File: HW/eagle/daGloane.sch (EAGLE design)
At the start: 61 parts, among them IC1 MCP1252-33X50, U1 STM32F10XTXU6, X2 SPARKFUN-CONNECTORS_USB-MICROB

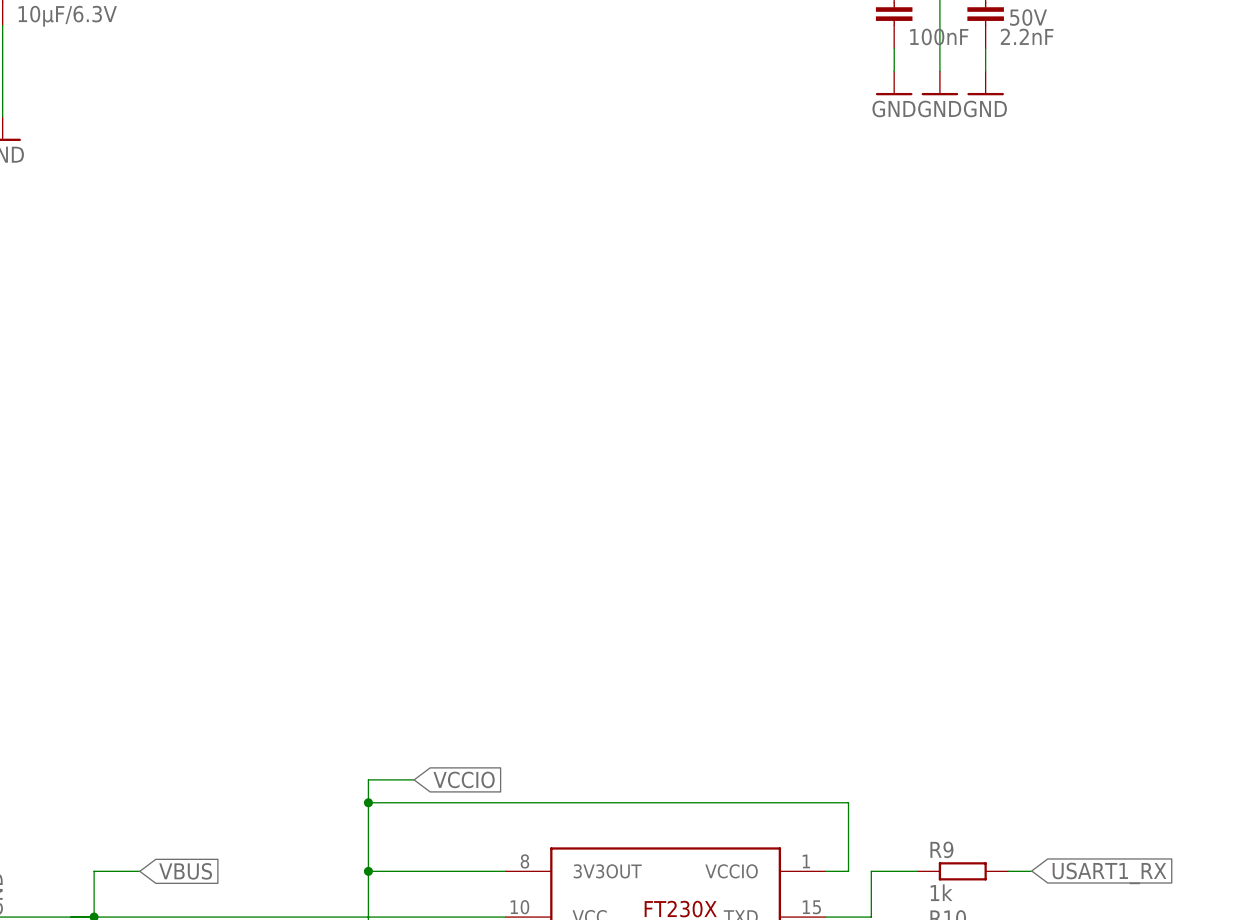
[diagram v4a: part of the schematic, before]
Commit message: Added Bluetooth module
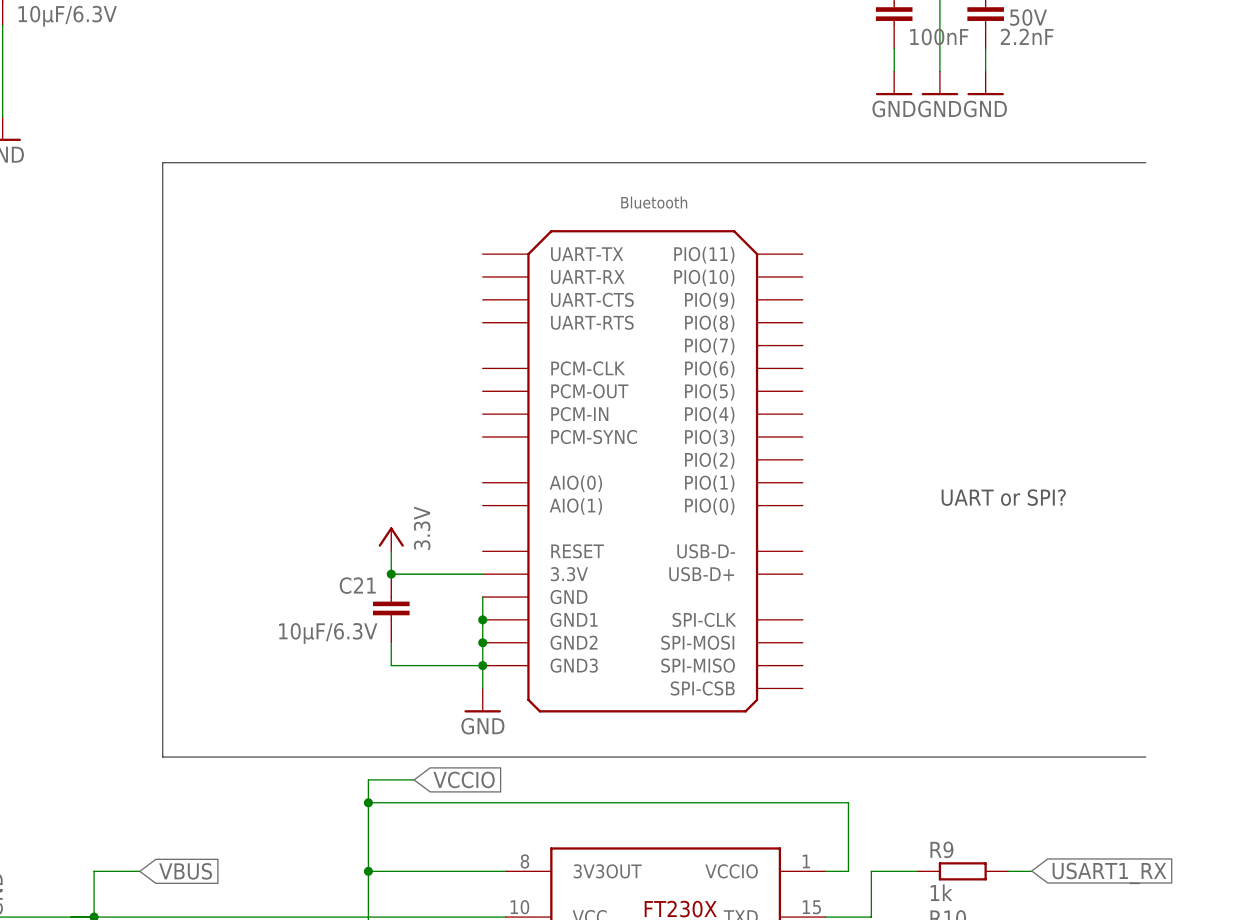
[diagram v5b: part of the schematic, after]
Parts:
- added C21: 10µF/6.3V, rcl:C-EUC0805
- added U$5: BLUETOOTH, daGloane:BLUETOOTH
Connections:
- net GND: now also C21.2, U$5.GND, U$5.GND1, U$5.GND2, U$5.GND3
- net VCC: now also C21.1, U$5.3.3V
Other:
- note added: "UART or SPI?"
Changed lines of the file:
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@@
 <layer number="95" name="Names" color="7" fill="1" visible="yes" active="yes"/>
 <layer number="96" name="Values" color="7" fill="1" visible="yes" active="yes"/>
-<layer number="97" name="Info" color="7" fill="1" visible="no" active="yes"/>
+<layer number="97" name="Info" color="7" fill="1" visible="yes" active="yes"/>
 <layer number="98" name="Guide" color="6" fill="1" visible="no" active="yes"/>
 <layer number="99" name="Anatomie" color="7" fill="1" visible="no" active="yes"/>
@@
 <part name="GND6" library="supply1" deviceset="GND" device=""/>
 <part name="X2" library="daGloane" deviceset="SPARKFUN-CONNECTORS_USB" device="-MICROB"/>
+<part name="U$5" library="daGloane" deviceset="BLUETOOTH" device=""/>
+<part name="C21" library="rcl" deviceset="C-EU" device="C0805" value="10µF/6.3V"/>
+<part name="3.3V1" library="supply1" deviceset="VCC" device="" value="3.3V"/>
+<part name="GND17" library="supply1" deviceset="GND" device=""/>
 </parts>
 <sheets>
@@
 <text x="215.9" y="15.24" size="2.54" layer="91">Filter hinter charge pump?</text>
 <text x="111.76" y="88.9" size="1.778" layer="91" rot="MR0">boot1</text>
+<wire x1="373.38" y1="147.32" x2="264.16" y2="147.32" width="0.1524" layer="97"/>
+<wire x1="264.16" y1="147.32" x2="264.16" y2="81.28" width="0.1524" layer="97"/>
+<wire x1="264.16" y1="81.28" x2="373.38" y2="81.28" width="0.1524" layer="97"/>
+<text x="350.52" y="109.22" size="1.778" layer="97">UART or SPI?</text>
 </plain>
 <instances>
@@
 <instance part="GND6" gate="1" x="116.84" y="17.78" rot="MR0"/>
 <instance part="X2" gate="G$1" x="233.68" y="66.04" rot="R180"/>
+<instance part="U$5" gate="G$1" x="325.12" y="121.92"/>
+<instance part="C21" gate="G$1" x="289.56" y="99.06" rot="MR0"/>
+<instance part="3.3V1" gate="VCC" x="289.56" y="106.68" rot="MR0"/>
+<instance part="GND17" gate="1" x="299.72" y="86.36" rot="MR0"/>
 </instances>
 <busses>
@@
 <wire x1="116.84" y1="25.4" x2="116.84" y2="20.32" width="0.1524" layer="91"/>
 <pinref part="GND6" gate="1" pin="GND"/>
+</segment>
+<segment>
+<pinref part="U$5" gate="G$1" pin="GND"/>
+<pinref part="U$5" gate="G$1" pin="GND1"/>
+<wire x1="299.72" y1="99.06" x2="299.72" y2="96.52" width="0.1524" layer="91"/>
+<pinref part="U$5" gate="G$1" pin="GND2"/>
+<wire x1="299.72" y1="96.52" x2="299.72" y2="93.98" width="0.1524" layer="91"/>
+<junction x="299.72" y="96.52"/>
+<pinref part="U$5" gate="G$1" pin="GND3"/>
+<wire x1="299.72" y1="93.98" x2="299.72" y2="91.44" width="0.1524" layer="91"/>
+<junction x="299.72" y="93.98"/>
+<wire x1="299.72" y1="91.44" x2="299.72" y2="88.9" width="0.1524" layer="91"/>
+<junction x="299.72" y="91.44"/>
+<pinref part="GND17" gate="1" pin="GND"/>
+<pinref part="C21" gate="G$1" pin="2"/>
+<wire x1="289.56" y1="93.98" x2="289.56" y2="91.44" width="0.1524" layer="91"/>
+<wire x1="289.56" y1="91.44" x2="299.72" y2="91.44" width="0.1524" layer="91"/>
 </segment>
 </net>
@@
 <wire x1="53.34" y1="175.26" x2="48.26" y2="175.26" width="0.1524" layer="91"/>
 </segment>
+<segment>
+<pinref part="C21" gate="G$1" pin="1"/>
+<pinref part="3.3V1" gate="VCC" pin="VCC"/>
+<wire x1="289.56" y1="104.14" x2="289.56" y2="101.6" width="0.1524" layer="91"/>
+<pinref part="U$5" gate="G$1" pin="3.3V"/>
+<wire x1="289.56" y1="101.6" x2="299.72" y2="101.6" width="0.1524" layer="91"/>
+<junction x="289.56" y="101.6"/>
+</segment>
 </net>

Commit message: Splitted schematic in Frames
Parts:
- added R22, R23: 1k, rcl:R-EU_R0603
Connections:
- new net N$15: R23.2, U$5.UART-RX
- new net N$7: R22.2, U$5.UART-TX
- net VCC: now also U$5.RESET
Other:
- note added: "Bluetooth"
- note added: "LIPO2PWR"
- note added: "Motion Tracking"
- note added: "PWR on/off"
- note added: "Power"
- note added: "Programming"
- note added: "USB2LIPO"
- note added: "communication"
- note added: "controller"
- note added: "easiest way to configure Module?"
- note removed: "UART or SPI?"
- moved on the sheet: BOOTMD, C1, C12, C13, C14, C15, C16, C17, C18, C19, C21, C4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

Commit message: missing connection uart connection to bluetooth module fixed
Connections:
- net USART2_RX: now also R22.1
- net USART2_TX: now also R23.1
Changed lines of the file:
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@@
 <?xml version="1.0" encoding="utf-8"?>
 <!DOCTYPE eagle SYSTEM "eagle.dtd">
-<eagle version="6.2">
+<eagle version="6.1">
 <drawing>
 <settings>
@@
 <wire x1="195.58" y1="-251.46" x2="193.04" y2="-251.46" width="0.1524" layer="91"/>
 <label x="193.04" y="-251.46" size="1.778" layer="95" rot="R180" xref="yes"/>
+<pinref part="R22" gate="G$1" pin="1"/>
 </segment>
 </net>
@@
 <wire x1="195.58" y1="-259.08" x2="193.04" y2="-259.08" width="0.1524" layer="91"/>
 <label x="193.04" y="-259.08" size="1.778" layer="95" rot="R180" xref="yes"/>
+<pinref part="R23" gate="G$1" pin="1"/>
 </segment>
 </net>

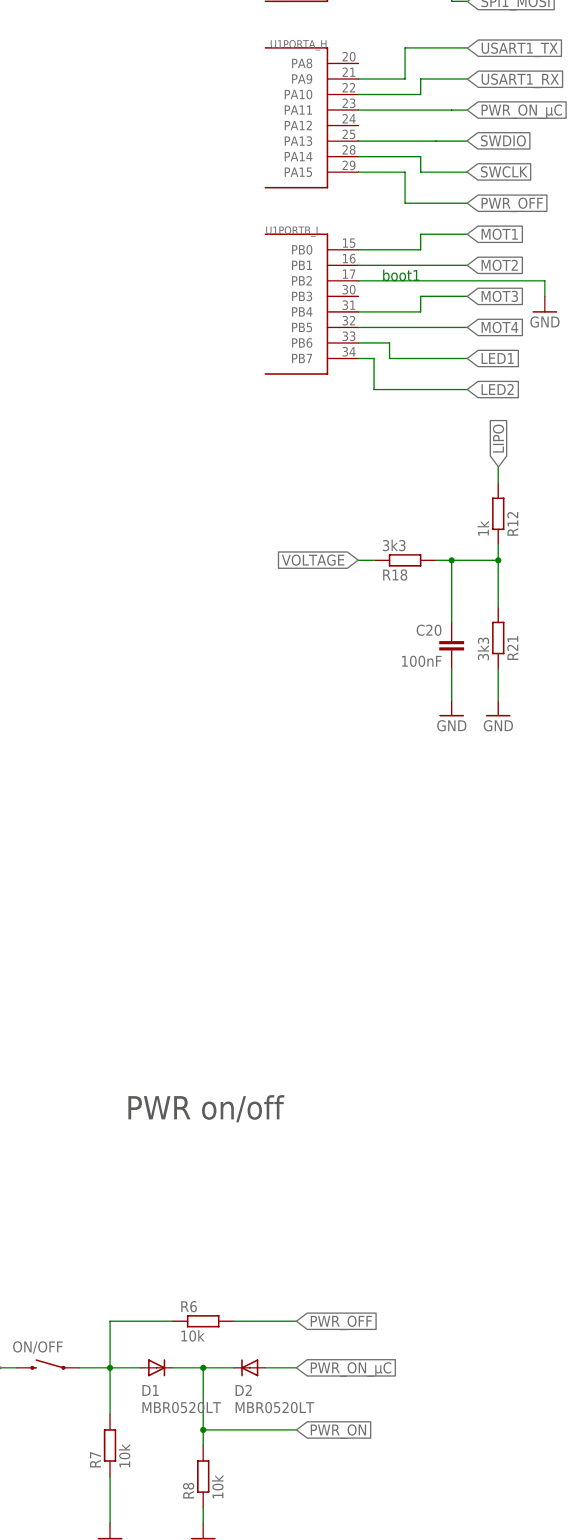
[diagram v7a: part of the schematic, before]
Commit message: 2 descrete diodes replaced by one part containing to diodes
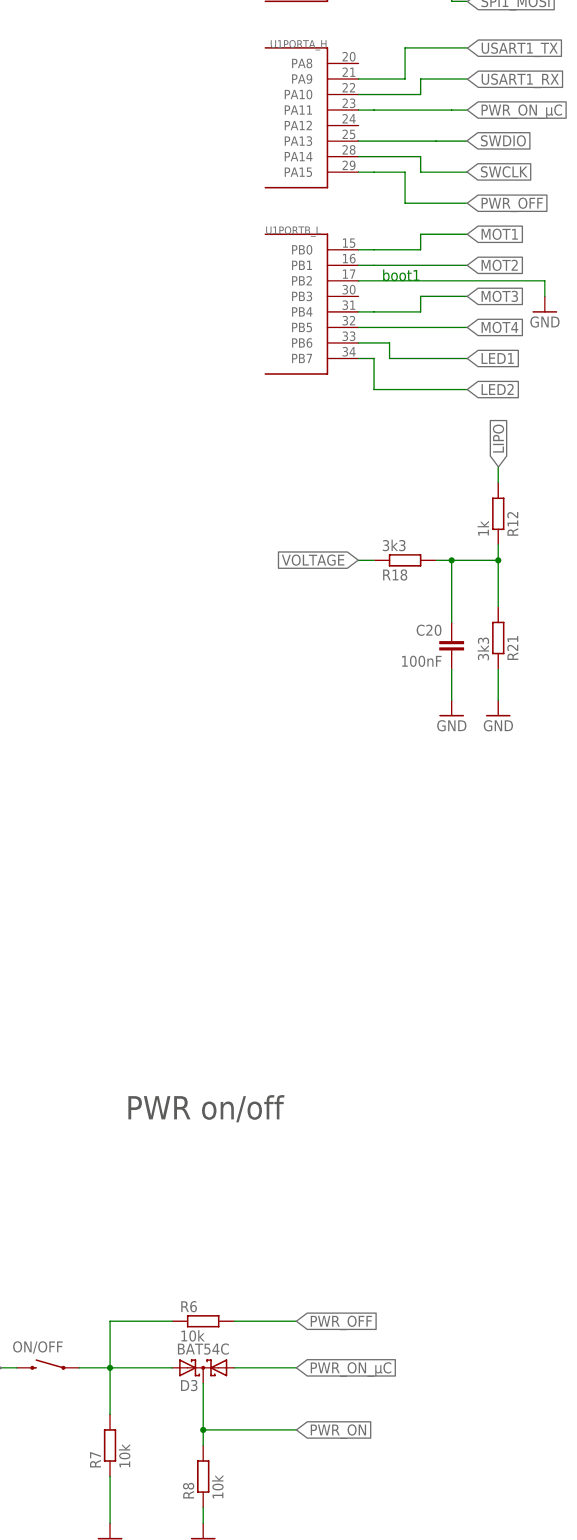
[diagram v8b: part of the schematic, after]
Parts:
- removed D1, D2: MBR0520LT, diode:MBR0520LT
- added D3: BAT54C, diode:BAT54C
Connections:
- new net MOT1: U1PORTB_L.PB0
- new net MOT2: U1PORTB_L.PB1
- new net MOT3: U1PORTB_L.PB4
- net N$23: now also D3.A2; no longer D1.A
- net PWR_OFF: now also U1PORTA_H.PA15
- net PWR_ON: now also D3.CC; no longer D1.C, D2.C
- net PWR_ON_µC: now also D3.A1, U1PORTA_H.PA11; no longer D2.A
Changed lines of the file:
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@@
 <?xml version="1.0" encoding="utf-8"?>
 <!DOCTYPE eagle SYSTEM "eagle.dtd">
-<eagle version="6.1">
+<eagle version="6.2">
 <drawing>
 <settings>
@@
 <part name="3.3V4" library="supply1" deviceset="VCC" device="" value="3.3V"/>
 <part name="ON/OFF" library="daGloane" deviceset="SWITCH-MOMENTARY-2" device="SMD"/>
-<part name="D1" library="diode" deviceset="MBR0520LT" device=""/>
 <part name="R7" library="rcl" deviceset="R-EU_" device="R0603" value="10k"/>
 <part name="GND35" library="supply1" deviceset="GND" device=""/>
 <part name="R6" library="rcl" deviceset="R-EU_" device="R0603" value="10k"/>
-<part name="D2" library="diode" deviceset="MBR0520LT" device=""/>
 <part name="R8" library="rcl" deviceset="R-EU_" device="R0603" value="10k"/>
 <part name="GND36" library="supply1" deviceset="GND" device=""/>
@@
 <part name="R22" library="rcl" deviceset="R-EU_" device="R0603" value="1k"/>
 <part name="R23" library="rcl" deviceset="R-EU_" device="R0603" value="1k"/>
+<part name="D3" library="diode" deviceset="BAT54C" device=""/>
 </parts>
 <sheets>
@@
 <attribute name="NAME" x="53.34" y="-86.36" size="1.778" layer="95" rot="MR0"/>
 </instance>
-<instance part="D1" gate="G$1" x="68.58" y="-88.9" smashed="yes">
-<attribute name="NAME" x="66.04" y="-93.4974" size="1.778" layer="95"/>
-<attribute name="VALUE" x="66.04" y="-96.2914" size="1.778" layer="96"/>
-</instance>
 <instance part="R7" gate="G$1" x="60.96" y="-101.6" rot="R90"/>
 <instance part="GND35" gate="1" x="60.96" y="-116.84"/>
 <instance part="R6" gate="G$1" x="76.2" y="-81.28"/>
-<instance part="D2" gate="G$1" x="83.82" y="-88.9" smashed="yes" rot="R180">
-<attribute name="NAME" x="81.28" y="-93.4974" size="1.778" layer="95"/>
-<attribute name="VALUE" x="81.28" y="-96.2914" size="1.778" layer="96"/>
-</instance>
 <instance part="R8" gate="G$1" x="76.2" y="-106.68" rot="R90"/>
 <instance part="GND36" gate="1" x="76.2" y="-116.84"/>
@@
 <instance part="R22" gate="G$1" x="200.66" y="-251.46"/>
 <instance part="R23" gate="G$1" x="200.66" y="-259.08"/>
+<instance part="D3" gate="G$1" x="76.2" y="-88.9" rot="R180"/>
 </instances>
 <busses>
@@
 <segment>
 <label x="91.44" y="-99.06" size="1.778" layer="95" xref="yes"/>
-<pinref part="D1" gate="G$1" pin="C"/>
-<wire x1="71.12" y1="-88.9" x2="76.2" y2="-88.9" width="0.1524" layer="91"/>
-<wire x1="76.2" y1="-88.9" x2="76.2" y2="-99.06" width="0.1524" layer="91"/>
 <wire x1="76.2" y1="-99.06" x2="91.44" y2="-99.06" width="0.1524" layer="91"/>
-<wire x1="76.2" y1="-88.9" x2="81.28" y2="-88.9" width="0.1524" layer="91"/>
-<pinref part="D2" gate="G$1" pin="C"/>
-<junction x="76.2" y="-88.9"/>
 <pinref part="R8" gate="G$1" pin="2"/>
 <wire x1="76.2" y1="-101.6" x2="76.2" y2="-99.06" width="0.1524" layer="91"/>
+<pinref part="D3" gate="G$1" pin="CC"/>
+<wire x1="76.2" y1="-99.06" x2="76.2" y2="-91.44" width="0.1524" layer="91"/>
 <junction x="76.2" y="-99.06"/>
 </segment>
@@
 </segment>
 <segment>
-<wire x1="101.6" y1="106.68" x2="109.22" y2="106.68" width="0.1524" layer="91"/>
+<wire x1="104.14" y1="106.68" x2="109.22" y2="106.68" width="0.1524" layer="91"/>
 <wire x1="109.22" y1="106.68" x2="109.22" y2="101.6" width="0.1524" layer="91"/>
 <wire x1="109.22" y1="101.6" x2="119.38" y2="101.6" width="0.1524" layer="91"/>
 <label x="119.38" y="101.6" size="1.778" layer="95" rot="MR180" xref="yes"/>
+<pinref part="U1" gate="PORTA_H" pin="PA15"/>
+<wire x1="101.6" y1="106.68" x2="104.14" y2="106.68" width="0.1524" layer="91"/>
 </segment>
 </net>
@@
 <segment>
 <pinref part="ON/OFF" gate="G$1" pin="1"/>
-<pinref part="D1" gate="G$1" pin="A"/>
-<wire x1="66.04" y1="-88.9" x2="60.96" y2="-88.9" width="0.1524" layer="91"/>
+<wire x1="71.12" y1="-88.9" x2="60.96" y2="-88.9" width="0.1524" layer="91"/>
 <wire x1="60.96" y1="-88.9" x2="55.88" y2="-88.9" width="0.1524" layer="91"/>
 <junction x="60.96" y="-88.9"/>
@@
 <wire x1="71.12" y1="-81.28" x2="60.96" y2="-81.28" width="0.1524" layer="91"/>
 <wire x1="60.96" y1="-81.28" x2="60.96" y2="-88.9" width="0.1524" layer="91"/>
+<pinref part="D3" gate="G$1" pin="A2"/>
 </segment>
 </net>
 <net name="PWR_ON_µC" class="0">
 <segment>
-<pinref part="D2" gate="G$1" pin="A"/>
-<wire x1="86.36" y1="-88.9" x2="91.44" y2="-88.9" width="0.1524" layer="91"/>
+<wire x1="81.28" y1="-88.9" x2="91.44" y2="-88.9" width="0.1524" layer="91"/>
 <label x="91.44" y="-88.9" size="1.778" layer="95" xref="yes"/>
+<pinref part="D3" gate="G$1" pin="A1"/>
 </segment>
 <segment>
-<wire x1="101.6" y1="116.84" x2="116.84" y2="116.84" width="0.1524" layer="91"/>
+<wire x1="104.14" y1="116.84" x2="116.84" y2="116.84" width="0.1524" layer="91"/>
 <wire x1="116.84" y1="116.84" x2="119.38" y2="116.84" width="0.1524" layer="91"/>
 <label x="119.38" y="116.84" size="1.778" layer="95" rot="MR180" xref="yes"/>
+<pinref part="U1" gate="PORTA_H" pin="PA11"/>
+<wire x1="101.6" y1="116.84" x2="104.14" y2="116.84" width="0.1524" layer="91"/>
 </segment>
 </net>
@@
 <net name="MOT2" class="0">
 <segment>
-<wire x1="101.6" y1="91.44" x2="119.38" y2="91.44" width="0.1524" layer="91"/>
+<wire x1="104.14" y1="91.44" x2="119.38" y2="91.44" width="0.1524" layer="91"/>
 <label x="119.38" y="91.44" size="1.778" layer="95" xref="yes"/>
+<pinref part="U1" gate="PORTB_L" pin="PB1"/>
+<wire x1="101.6" y1="91.44" x2="104.14" y2="91.44" width="0.1524" layer="91"/>
 </segment>
 </net>
 <net name="MOT3" class="0">
 <segment>
-<wire x1="101.6" y1="83.82" x2="111.76" y2="83.82" width="0.1524" layer="91"/>
+<wire x1="104.14" y1="83.82" x2="111.76" y2="83.82" width="0.1524" layer="91"/>
 <wire x1="111.76" y1="83.82" x2="111.76" y2="86.36" width="0.1524" layer="91"/>
 <wire x1="111.76" y1="86.36" x2="119.38" y2="86.36" width="0.1524" layer="91"/>
 <label x="119.38" y="86.36" size="1.778" layer="95" xref="yes"/>
+<pinref part="U1" gate="PORTB_L" pin="PB4"/>
+<wire x1="101.6" y1="83.82" x2="104.14" y2="83.82" width="0.1524" layer="91"/>
 </segment>
 </net>
 <net name="MOT1" class="0">
 <segment>
-<wire x1="101.6" y1="93.98" x2="111.76" y2="93.98" width="0.1524" layer="91"/>
+<wire x1="104.14" y1="93.98" x2="111.76" y2="93.98" width="0.1524" layer="91"/>
 <wire x1="111.76" y1="93.98" x2="111.76" y2="96.52" width="0.1524" layer="91"/>
 <wire x1="111.76" y1="96.52" x2="119.38" y2="96.52" width="0.1524" layer="91"/>
 <label x="119.38" y="96.52" size="1.778" layer="95" xref="yes"/>
+<pinref part="U1" gate="PORTB_L" pin="PB0"/>
+<wire x1="101.6" y1="93.98" x2="104.14" y2="93.98" width="0.1524" layer="91"/>
 </segment>
 </net>
